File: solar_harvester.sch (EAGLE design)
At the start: 46 parts, among them U1 BQ25505, U2 TPS61322XA, U3 TPS61322XA, U4 MAX17040, U5 INA226, U6 DMP3085LSD

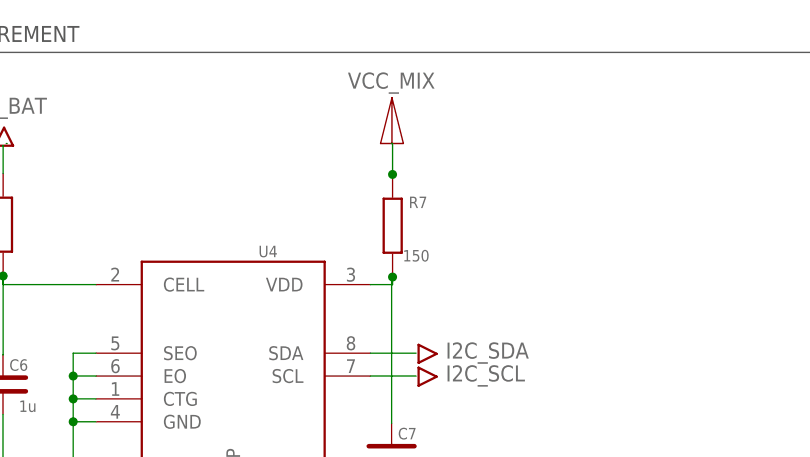
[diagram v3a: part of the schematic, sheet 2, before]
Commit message: final BOM Rev0 composed, layout adjust
Some caps sizes were changed due to vol/dimension issues
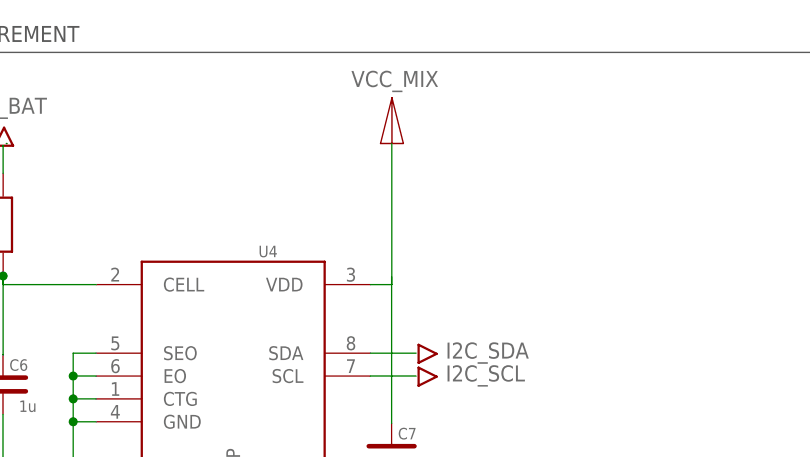
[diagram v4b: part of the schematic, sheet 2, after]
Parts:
- removed R7: 150, vrlib_res:RESISITOR_0603
- C11: device vrlib_caps:0603_CERAMIC -> vrlib_caps:1005_CER
- C3: device vrlib_caps:0603_CERAMIC -> vrlib_caps:2012_CER
- R8: device vrlib_res:RESISITOR_0603 -> vrlib_res:RESISTOR_2012
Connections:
- removed net N$7: C7.1, R7.P$1, U4.VDD
- net VCC_MIX: now also C7.1, U4.VDD; no longer R7.P$2
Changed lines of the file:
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@@
 <setting verticaltext="up"/>
 </settings>
-<grid distance="0.1" unitdist="inch" unit="inch" style="lines" multiple="1" display="no" altdistance="0.01" altunitdist="inch" altunit="inch"/>
+<grid distance="1" unitdist="mm" unit="mm" style="lines" multiple="1" display="no" altdistance="0.1" altunitdist="mm" altunit="mm"/>
 <layers>
-<layer number="1" name="Top" color="4" fill="1" visible="no" active="no"/>
-<layer number="16" name="Bottom" color="1" fill="1" visible="no" active="no"/>
-<layer number="17" name="Pads" color="2" fill="1" visible="no" active="no"/>
-<layer number="18" name="Vias" color="2" fill="1" visible="no" active="no"/>
-<layer number="19" name="Unrouted" color="6" fill="1" visible="no" active="no"/>
-<layer number="20" name="Dimension" color="15" fill="1" visible="no" active="no"/>
-<layer number="21" name="tPlace" color="7" fill="1" visible="no" active="no"/>
-<layer number="22" name="bPlace" color="7" fill="1" visible="no" active="no"/>
-<layer number="23" name="tOrigins" color="15" fill="1" visible="no" active="no"/>
-<layer number="24" name="bOrigins" color="15" fill="1" visible="no" active="no"/>
-<layer number="25" name="tNames" color="7" fill="1" visible="no" active="no"/>
-<layer number="26" name="bNames" color="7" fill="1" visible="no" active="no"/>
-<layer number="27" name="tValues" color="7" fill="1" visible="no" active="no"/>
-<layer number="28" name="bValues" color="7" fill="1" visible="no" active="no"/>
+<layer number="1" name="Top" color="4" fill="1" visible="yes" active="no"/>
+<layer number="16" name="Bottom" color="1" fill="1" visible="yes" active="no"/>
+<layer number="17" name="Pads" color="2" fill="1" visible="yes" active="no"/>
+<layer number="18" name="Vias" color="2" fill="1" visible="yes" active="no"/>
+<layer number="19" name="Unrouted" color="6" fill="1" visible="yes" active="no"/>
+<layer number="20" name="Dimension" color="24" fill="1" visible="yes" active="no"/>
+<layer number="21" name="tPlace" color="7" fill="1" visible="yes" active="no"/>
+<layer number="22" name="bPlace" color="7" fill="1" visible="yes" active="no"/>
+<layer number="23" name="tOrigins" color="15" fill="1" visible="yes" active="no"/>
+<layer number="24" name="bOrigins" color="15" fill="1" visible="yes" active="no"/>
+<layer number="25" name="tNames" color="7" fill="1" visible="yes" active="no"/>
+<layer number="26" name="bNames" color="7" fill="1" visible="yes" active="no"/>
+<layer number="27" name="tValues" color="7" fill="1" visible="yes" active="no"/>
+<layer number="28" name="bValues" color="7" fill="1" visible="yes" active="no"/>
 <layer number="29" name="tStop" color="7" fill="3" visible="no" active="no"/>
 <layer number="30" name="bStop" color="7" fill="6" visible="no" active="no"/>
@@
 <layer number="35" name="tGlue" color="7" fill="4" visible="no" active="no"/>
 <layer number="36" name="bGlue" color="7" fill="5" visible="no" active="no"/>
-<layer number="37" name="tTest" color="7" fill="1" visible="no" active="no"/>
-<layer number="38" name="bTest" color="7" fill="1" visible="no" active="no"/>
+<layer number="37" name="tTest" color="7" fill="1" visible="yes" active="no"/>
+<layer number="38" name="bTest" color="7" fill="1" visible="yes" active="no"/>
 <layer number="39" name="tKeepout" color="4" fill="11" visible="no" active="no"/>
 <layer number="40" name="bKeepout" color="1" fill="11" visible="no" active="no"/>
@@
 <layer number="44" name="Drills" color="7" fill="1" visible="no" active="no"/>
 <layer number="45" name="Holes" color="7" fill="1" visible="no" active="no"/>
-<layer number="46" name="Milling" color="3" fill="1" visible="no" active="no"/>
-<layer number="47" name="Measures" color="7" fill="1" visible="no" active="no"/>
-<layer number="48" name="Document" color="7" fill="1" visible="no" active="no"/>
-<layer number="49" name="Reference" color="7" fill="1" visible="no" active="no"/>
-<layer number="51" name="tDocu" color="7" fill="1" visible="no" active="no"/>
-<layer number="52" name="bDocu" color="7" fill="1" visible="no" active="no"/>
+<layer number="46" name="Milling" color="3" fill="1" visible="yes" active="no"/>
+<layer number="47" name="Measures" color="7" fill="1" visible="yes" active="no"/>
+<layer number="48" name="Document" color="7" fill="1" visible="yes" active="no"/>
+<layer number="49" name="Reference" color="7" fill="1" visible="yes" active="no"/>
+<layer number="51" name="tDocu" color="7" fill="1" visible="yes" active="no"/>
+<layer number="52" name="bDocu" color="7" fill="1" visible="yes" active="no"/>
 <layer number="88" name="SimResults" color="9" fill="1" visible="yes" active="yes"/>
 <layer number="89" name="SimProbes" color="9" fill="1" visible="yes" active="yes"/>
@@
 <part name="C2" library="vrlib_caps" deviceset="0603_CERAMIC" device="" value="4u7"/>
 <part name="U$6" library="vrlib_com_symbols" deviceset="GND" device=""/>
-<part name="C3" library="vrlib_caps" deviceset="0603_CERAMIC" device="" value="100u"/>
+<part name="C3" library="vrlib_caps" deviceset="2012_CER" device="" value="100u"/>
 <part name="PV_IN" library="vrlib_connector" deviceset="CONN_SCEW_TYPE_2P" device=""/>
 <part name="U$8" library="vrlib_com_symbols" deviceset="GND" device=""/>
@@
 <part name="R6" library="vrlib_res" deviceset="RESISITOR_0603" device="" value="1K"/>
 <part name="C6" library="vrlib_caps" deviceset="0603_CERAMIC" device="" value="1u"/>
-<part name="R7" library="vrlib_res" deviceset="RESISITOR_0603" device="" value="150"/>
 <part name="U$2" library="vrlib_com_symbols" deviceset="LOUT" device=""/>
 <part name="U$3" library="vrlib_com_symbols" deviceset="LOUT" device=""/>
@@
 <part name="U$4" library="vrlib_com_symbols" deviceset="GND" device=""/>
 <part name="U$12" library="vrlib_com_symbols" deviceset="GND" device=""/>
-<part name="R8" library="vrlib_res" deviceset="RESISITOR_0603" device="" value="2m"/>
+<part name="R8" library="vrlib_res" deviceset="RESISTOR_2012" device="" value="2m"/>
 <part name="U$13" library="vrlib_com_symbols" deviceset="LOUT" device=""/>
 <part name="U$15" library="vrlib_com_symbols" deviceset="LOUT" device=""/>
@@
 <part name="U$27" library="vrlib_com_symbols" deviceset="LOUT" device=""/>
 <part name="U$28" library="vrlib_com_symbols" deviceset="GND" device=""/>
-<part name="C11" library="vrlib_caps" deviceset="0603_CERAMIC" device="" value="10u"/>
+<part name="C11" library="vrlib_caps" deviceset="1005_CER" device="" value="10u"/>
 <part name="D1" library="vrlib_diode" deviceset="JDH2S02SL" device=""/>
 <part name="U$29" library="vrlib_com_symbols" deviceset="LOUT" device=""/>
@@
 <attribute name="VALUE" x="36.046" y="128.164" size="1.27" layer="96" rot="R180"/>
 </instance>
-<instance part="R7" gate="G$1" x="75.6" y="147.582" smashed="yes" rot="R90">
-<attribute name="NAME" x="79.46" y="150.814" size="1.27" layer="95" rot="R180"/>
-<attribute name="VALUE" x="79.698" y="144.882" size="1.27" layer="96" rot="R180"/>
-</instance>
 <instance part="U$2" gate="G$1" x="78.48" y="133.35" smashed="yes" rot="R270"/>
 <instance part="U$3" gate="G$1" x="78.48" y="130.81" smashed="yes" rot="R270"/>
@@
 <wire x1="32.316" y1="141.04" x2="32.316" y2="141.998" width="0.1524" layer="91"/>
 <junction x="32.316" y="141.998"/>
-</segment>
-</net>
-<net name="N$7" class="0">
-<segment>
-<pinref part="C7" gate="G$1" pin="1"/>
-<pinref part="R7" gate="G$1" pin="P$1"/>
-<wire x1="75.48" y1="125.624" x2="75.48" y2="141.882" width="0.1524" layer="91"/>
-<wire x1="75.48" y1="141.882" x2="75.584" y2="141.882" width="0.1524" layer="91"/>
-<pinref part="U4" gate="G$1" pin="VDD"/>
-<wire x1="73.12" y1="141.04" x2="75.584" y2="141.04" width="0.1524" layer="91"/>
-<wire x1="75.584" y1="141.04" x2="75.584" y2="141.882" width="0.1524" layer="91"/>
-<junction x="75.584" y="141.882"/>
 </segment>
 </net>
@@
 <net name="VCC_MIX" class="0">
 <segment>
-<wire x1="75.584" y1="156.718" x2="75.438" y2="156.718" width="0.1524" layer="91"/>
-<pinref part="R7" gate="G$1" pin="P$2"/>
-<wire x1="75.584" y1="153.398" x2="75.584" y2="153.282" width="0.1524" layer="91"/>
-<wire x1="75.584" y1="153.282" x2="75.584" y2="156.718" width="0.1524" layer="91"/>
-<junction x="75.584" y="153.282"/>
-<label x="70.612" y="162.814" size="1.778" layer="95"/>
-</segment>
-<segment>
 <pinref part="U5" gate="G$1" pin="VS"/>
 <wire x1="177.26" y1="146.68" x2="172.18" y2="146.68" width="0.1524" layer="91"/>
@@
 <label x="112.346" y="73.708" size="1.778" layer="95"/>
 </segment>
-</net>
+<segment>
+<pinref part="U4" gate="G$1" pin="VDD"/>
+<wire x1="73.12" y1="141.04" x2="75.5" y2="141.04" width="0.1524" layer="91"/>
+<wire x1="75.5" y1="141.04" x2="75.5" y2="156.7" width="0.1524" layer="91"/>
+<label x="71" y="163" size="1.778" layer="95"/>
+</segment>
+<segment>
+<pinref part="C7" gate="G$1" pin="1"/>
+<wire x1="75.48" y1="125.624" x2="75.48" y2="141.882" width="0.1524" layer="91"/>
+</segment>
+</net>

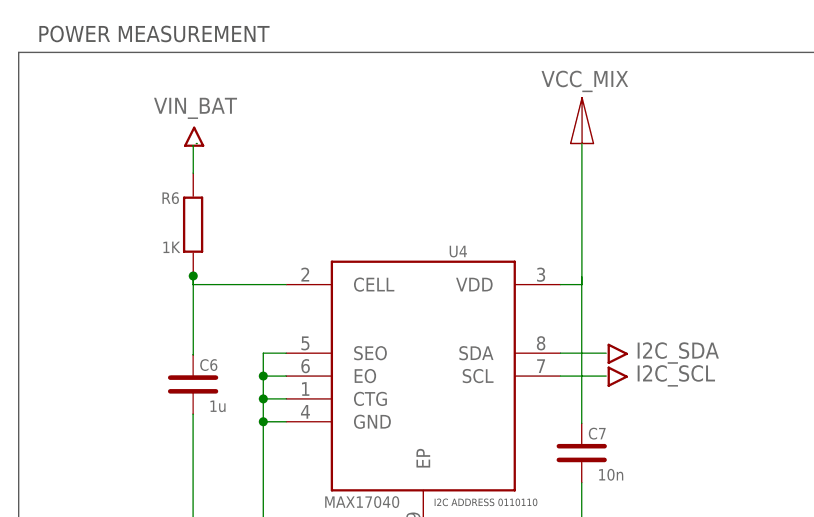
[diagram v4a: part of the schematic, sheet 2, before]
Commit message: increase comps sizes -> pcb reruting (in progress)
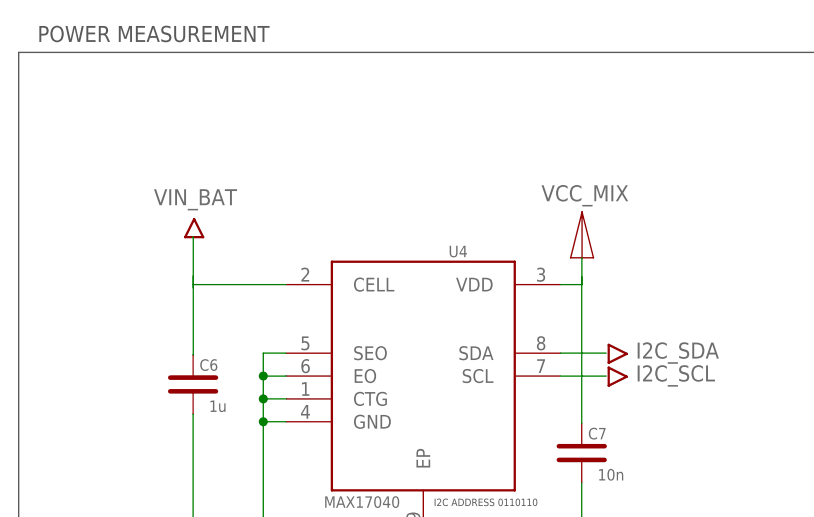
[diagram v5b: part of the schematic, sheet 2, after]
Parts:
- removed R6: 1K, vrlib_res:RESISITOR_0603
- C1, C2, C4, C5, C6, C7, C8: device vrlib_caps:0603_CERAMIC -> vrlib_caps:1608_CAP
- D1: value JDH2S02SL -> SD101BW; device vrlib_diode:JDH2S02SL -> vrlib_diode:SD101BW
- R1, R2, R3, R4, R5, R9: device vrlib_res:RESISITOR_0603 -> vrlib_res:RESISTOR_1608
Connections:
- removed net N$8: C6.1, R6.P$2, U4.CELL
- removed net N$9: D1.P$2, PV_IN.VIN
- new net N$7: D1.2, PV_IN.VIN
- net PVIN: now also D1.1; no longer D1.P$1
- net VIN_BAT: now also C6.1, U4.CELL; no longer R6.P$1

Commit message: BOM updated
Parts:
- R3: value 7.32M -> 1.2M
- R4: value 7.32M -> 7.5M
- R5: value 7.32M -> 4.3M
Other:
- note added: "MPPT"
- note added: "Over-voltage"
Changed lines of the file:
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@@
 <part name="R1" library="vrlib_res" deviceset="RESISTOR_1608" device="" value="7.32M"/>
 <part name="R2" library="vrlib_res" deviceset="RESISTOR_1608" device="" value="5.62M"/>
-<part name="R3" library="vrlib_res" deviceset="RESISTOR_1608" device="" value="7.32M"/>
-<part name="R4" library="vrlib_res" deviceset="RESISTOR_1608" device="" value="7.32M"/>
-<part name="R5" library="vrlib_res" deviceset="RESISTOR_1608" device="" value="7.32M"/>
+<part name="R3" library="vrlib_res" deviceset="RESISTOR_1608" device="" value="1.2M"/>
+<part name="R4" library="vrlib_res" deviceset="RESISTOR_1608" device="" value="7.5M"/>
+<part name="R5" library="vrlib_res" deviceset="RESISTOR_1608" device="" value="4.3M"/>
 <part name="U$17" library="vrlib_com_symbols" deviceset="LOUT" device=""/>
 <part name="L2" library="vrlib_induc" deviceset="FIXED_5050" device="" value="4u7"/>
@@
 <wire x1="116.84" y1="66.04" x2="177.8" y2="66.04" width="0.1524" layer="97"/>
 <text x="118" y="67" size="1.778" layer="97">POWER OUTPUT</text>
+<text x="30.48" y="109.22" size="1.778" layer="97" rot="R90">Over-voltage</text>
+<text x="43.18" y="101.6" size="1.778" layer="97" rot="R90">MPPT</text>
 </plain>
 <instances>

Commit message: Rev2
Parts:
- added FID3, FID4: FIDUCIAL_25, vrlib_prod:FIDUCIAL_25
- C10, C9: value 22u -> 100u; device vrlib_caps:1608_CAP -> vrlib_caps:3528_POL_CAP
- C11: device vrlib_caps:1005_CER -> vrlib_caps:1608_CAP
- C3: device vrlib_caps:2012_CER -> vrlib_caps:3528_POL_CAP
- renumbered 3V3_OUT to --3V3_OUT+, 5V_OUT to --5V_OUT+, BAT_IN to +BAT_IN--, PV_IN to +PV_IN--
